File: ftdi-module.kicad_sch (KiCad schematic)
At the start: 58 parts, among them U1 AP62301WU-7, U2 FT4232H_VQFN, U3 AP62301WU-7, Y1 Resonator_12MHz_ABM8G

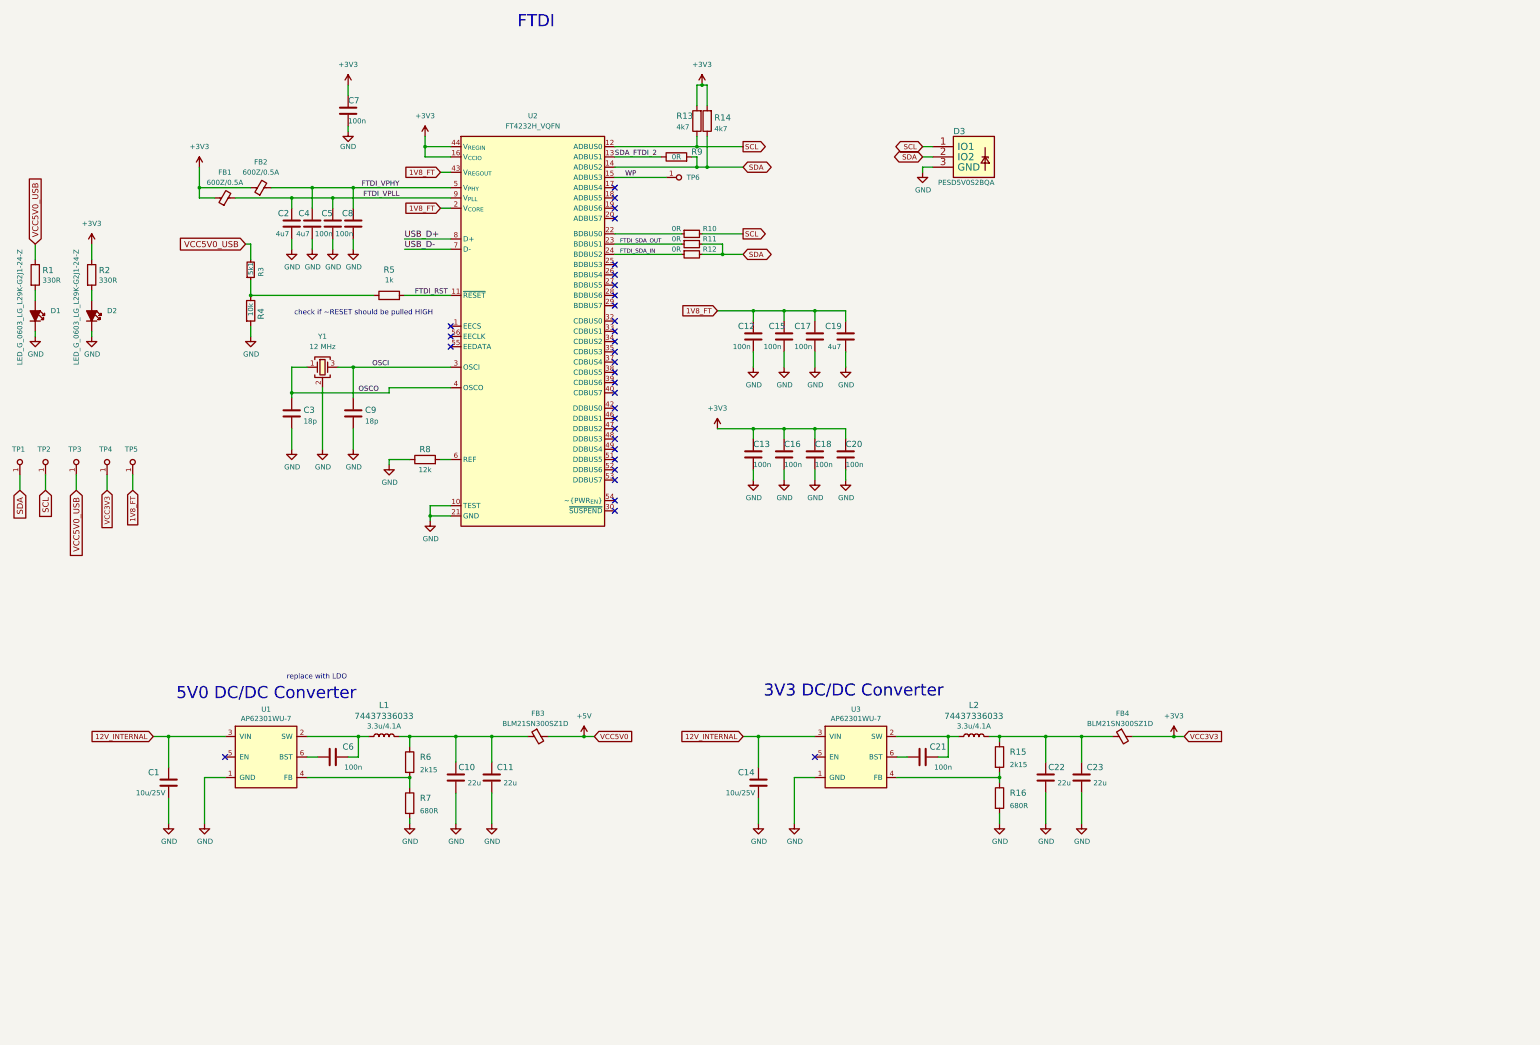
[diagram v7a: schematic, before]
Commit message: Set resitsors to standard
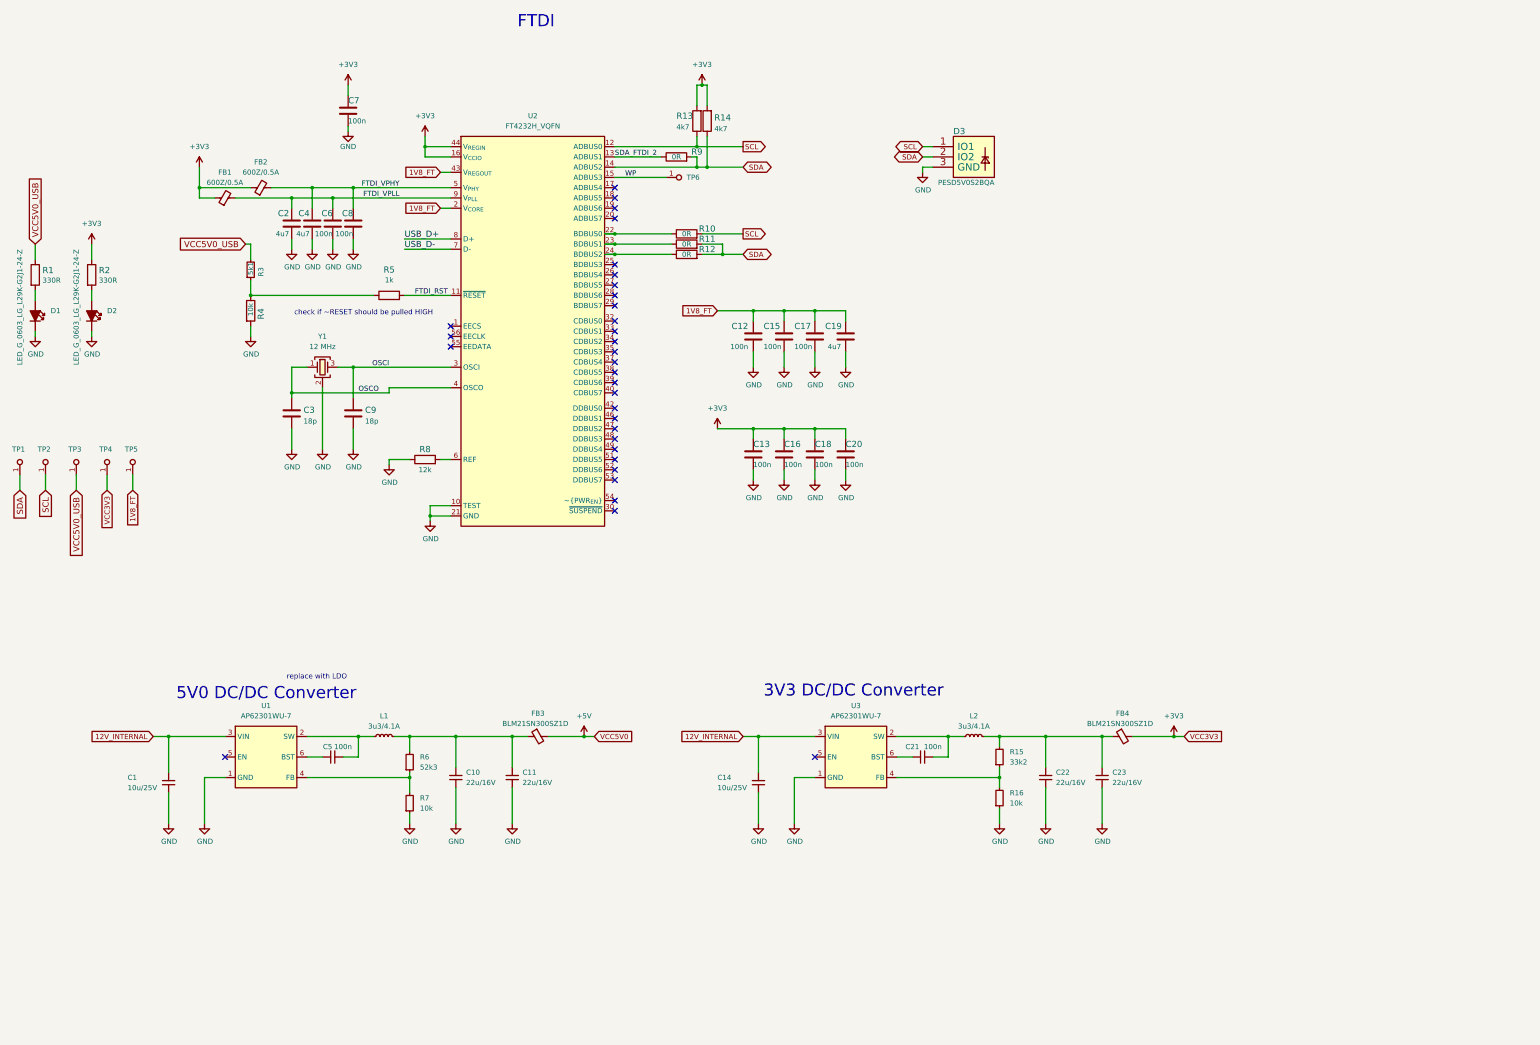
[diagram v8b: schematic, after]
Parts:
- removed C1, C14: C_10u_16V_0603, d1600e-psu-breakout-board-footprints:0603-cap, symbol d1600e-psu-breakout-board:C_10u_25V_0603
- removed C10, C11, C22, C23: C_22u_0603, d1600e-psu-breakout-board-footprints:0603-cap, symbol d1600e-psu-breakout-board:C_22u_0603
- removed C21, C6: C_100n_0402, d1600e-psu-breakout-board-footprints:0402-cap, symbol d1600e-psu-breakout-board:C_100n_0402
- removed L1, L2: 74437336033, d1600e-psu-breakout-board-footprints:WE_74437336033, symbol d1600e-psu-breakout-board:74437336033
- removed R10, R11, R12: R_0R_0402, nuc-compute-cluster-environment-sensor-footprints:R_0402_1005Metric, symbol nuc-compute-cluster-environment-sensor:R_0R_0402
- removed R15, R6: R_2k15_0402, antmicro-footprints:0402-res, symbol antmicroResistors0402:R_2k15_0402
- removed R16, R7: R_680R_0402, antmicro-footprints:0402-res, symbol antmicroResistors0402:R_680R_0402
- removed U1, U3: AP62301WU-7, d1600e-psu-breakout-board-footprints:TSOT23-6, symbol d1600e-psu-breakout-board:AP62301WU-7
- added C1, C14: C_10u_25V_0603, antmicro-footprints:C_0603_1608Metric, symbol antmicroCapacitors0603:C_10u_25V_0603
- added C10, C11, C22, C23: C_22u_16V_0603, antmicro-footprints:C_0603_1608Metric, symbol antmicroCapacitors0603:C_22u_16V_0603
- added C21, C5: C_100n_0402, antmicro-footprints:C_0402_1005Metric, symbol antmicroCapacitors0402:C_100n_0402
- added L1, L2: L_3u3_4.1A_WE-LHMI-5030, antmicro-footprints:L_WE-LHMI-5030, symbol antmicroFixedInductors:L_3u3_4.1A_WE-LHMI-5030
- added R10, R11, R12: R_0R_0603, antmicro-footprints:R_0603_1608Metric, symbol antmicroResistors0603:R_0R_0603
- added R15: R_33k2_0402, antmicro-footprints:R_0402_1005Metric, symbol antmicroResistors0402:R_33k2_0402
- added R16, R7: R_10k_0402, antmicro-footprints:R_0402_1005Metric, symbol antmicroResistors0402:R_10k_0402
- added R6: R_52k3_0402, antmicro-footprints:R_0402_1005Metric, symbol antmicroResistors0402:R_52k3_0402
- added U1, U3: AP62301_TSOT, antmicro-footprints:TSOT23-6, symbol antmicroDCDCConverters:AP62301_TSOT
- renumbered C5 to C6
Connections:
- net 12V_INTERNAL: now also C1.2, C14.2, U1.3 (VIN), U3.3 (VIN)
- net GND: now also C1.1, C10.1, C11.1, C14.1, C22.1, C23.1, R16.1, R7.1, U1.1 (GND), U3.1 (GND)
- net SCL: now also R10.2
- net SDA: now also R11.2, R12.2
- net at FB4.1: now also C22.2, C23.2, L2.2, R15.2
- net at U2.22 (BDBUS0): now also R10.1
- net at FB3.1: now also C10.2, C11.2, L1.2, R6.2
- net FTDI_SDA_IN: no longer names the net of U2.24 (BDBUS2)
- net FTDI_SDA_IN: now also R12.1
- net FTDI_SDA_OUT: no longer names the net of U2.23 (BDBUS1)
- net FTDI_SDA_OUT: now also R11.1
- new net: C21.1, U3.6 (BST)
- new net: C21.2, L2.1, U3.2 (SW)
- new net: R15.1, R16.2, U3.4 (FB)
- new net: C5.2, L1.1, U1.2 (SW)
- new net: R6.1, R7.2, U1.4 (FB)
- new net: C5.1, U1.6 (BST)
